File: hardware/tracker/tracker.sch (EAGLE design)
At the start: 2 parts, among them X1 MINI-USB-SHIELD-UX60-MB-5ST

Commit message: Parts libraries started
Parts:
- added U$2: BMP085, bmp085:BMP085
- added U$3: CC2540-MINI-BLE, cc2540:CC2540-MINI-BLE
- X1: value MINI-USB-SHIELD-UX60-MB-5ST -> MINI-USB-SCHIELD-32005-301; device con-hirose:MINI-USB-SHIELD-UX60-MB-5ST -> con-cypressindustries:MINI-USB-SCHIELD-32005-301
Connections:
- new net +5V: X1G$1.1
- new net GND: X1G$1.5, X1S.S1, X1S.S2, X1S.S3, X1S.S4
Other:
- moved on the sheet: U$1
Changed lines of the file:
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@@
 <grid distance="0.1" unitdist="inch" unit="inch" style="lines" multiple="1" display="no" altdistance="0.01" altunitdist="inch" altunit="inch"/>
 <layers>
-<layer number="1" name="Top" color="4" fill="1" visible="yes" active="no"/>
-<layer number="16" name="Bottom" color="1" fill="1" visible="yes" active="no"/>
-<layer number="17" name="Pads" color="2" fill="1" visible="yes" active="no"/>
-<layer number="18" name="Vias" color="2" fill="1" visible="yes" active="no"/>
-<layer number="19" name="Unrouted" color="6" fill="1" visible="yes" active="no"/>
-<layer number="20" name="Dimension" color="15" fill="1" visible="yes" active="no"/>
-<layer number="21" name="tPlace" color="7" fill="1" visible="yes" active="no"/>
-<layer number="22" name="bPlace" color="7" fill="1" visible="yes" active="no"/>
-<layer number="23" name="tOrigins" color="15" fill="1" visible="yes" active="no"/>
-<layer number="24" name="bOrigins" color="15" fill="1" visible="yes" active="no"/>
-<layer number="25" name="tNames" color="7" fill="1" visible="yes" active="no"/>
-<layer number="26" name="bNames" color="7" fill="1" visible="yes" active="no"/>
-<layer number="27" name="tValues" color="7" fill="1" visible="yes" active="no"/>
-<layer number="28" name="bValues" color="7" fill="1" visible="yes" active="no"/>
+<layer number="1" name="Top" color="4" fill="1" visible="no" active="no"/>
+<layer number="16" name="Bottom" color="1" fill="1" visible="no" active="no"/>
+<layer number="17" name="Pads" color="2" fill="1" visible="no" active="no"/>
+<layer number="18" name="Vias" color="2" fill="1" visible="no" active="no"/>
+<layer number="19" name="Unrouted" color="6" fill="1" visible="no" active="no"/>
+<layer number="20" name="Dimension" color="15" fill="1" visible="no" active="no"/>
+<layer number="21" name="tPlace" color="7" fill="1" visible="no" active="no"/>
+<layer number="22" name="bPlace" color="7" fill="1" visible="no" active="no"/>
+<layer number="23" name="tOrigins" color="15" fill="1" visible="no" active="no"/>
+<layer number="24" name="bOrigins" color="15" fill="1" visible="no" active="no"/>
+<layer number="25" name="tNames" color="7" fill="1" visible="no" active="no"/>
+<layer number="26" name="bNames" color="7" fill="1" visible="no" active="no"/>
+<layer number="27" name="tValues" color="7" fill="1" visible="no" active="no"/>
+<layer number="28" name="bValues" color="7" fill="1" visible="no" active="no"/>
 <layer number="29" name="tStop" color="7" fill="3" visible="no" active="no"/>
 <layer number="30" name="bStop" color="7" fill="6" visible="no" active="no"/>
@@
 <layer number="35" name="tGlue" color="7" fill="4" visible="no" active="no"/>
 <layer number="36" name="bGlue" color="7" fill="5" visible="no" active="no"/>
-<layer number="37" name="tTest" color="7" fill="1" visible="yes" active="no"/>
-<layer number="38" name="bTest" color="7" fill="1" visible="yes" active="no"/>
+<layer number="37" name="tTest" color="7" fill="1" visible="no" active="no"/>
+<layer number="38" name="bTest" color="7" fill="1" visible="no" active="no"/>
 <layer number="39" name="tKeepout" color="4" fill="11" visible="no" active="no"/>
 <layer number="40" name="bKeepout" color="1" fill="11" visible="no" active="no"/>
@@
 <layer number="44" name="Drills" color="7" fill="1" visible="no" active="no"/>
 <layer number="45" name="Holes" color="7" fill="1" visible="no" active="no"/>
-<layer number="46" name="Milling" color="3" fill="1" visible="yes" active="no"/>
-<layer number="47" name="Measures" color="7" fill="1" visible="yes" active="no"/>
-<layer number="48" name="Document" color="7" fill="1" visible="yes" active="no"/>
-<layer number="49" name="Reference" color="7" fill="1" visible="yes" active="no"/>
-<layer number="51" name="tDocu" color="7" fill="1" visible="yes" active="no"/>
-<layer number="52" name="bDocu" color="7" fill="1" visible="yes" active="no"/>
+<layer number="46" name="Milling" color="3" fill="1" visible="no" active="no"/>
+<layer number="47" name="Measures" color="7" fill="1" visible="no" active="no"/>
+<layer number="48" name="Document" color="7" fill="1" visible="no" active="no"/>
+<layer number="49" name="Reference" color="7" fill="1" visible="no" active="no"/>
+<layer number="51" name="tDocu" color="7" fill="1" visible="no" active="no"/>
+<layer number="52" name="bDocu" color="7" fill="1" visible="no" active="no"/>
 <layer number="91" name="Nets" color="2" fill="1" visible="yes" active="yes"/>
 <layer number="92" name="Busses" color="1" fill="1" visible="yes" active="yes"/>
@@
 <class number="0" name="default" width="0" drill="0">
 </class>
+<class number="1" name="VCC" width="0.3" drill="0">
+</class>
+<class number="2" name="GND" width="0.5" drill="0">
+</class>
+<class number="3" name="+5V" width="0.5" drill="0">
+</class>
 </classes>
 <parts>
-<part name="X1" library="con-hirose" deviceset="MINI-USB-SHIELD-" device="UX60-MB-5ST"/>
 <part name="U$1" library="adxl345" deviceset="ADXL345" device=""/>
+<part name="X1" library="con-cypressindustries" deviceset="MINI-USB-SCHIELD-" device="32005-301"/>
+<part name="GND1" library="supply1" deviceset="GND" device=""/>
+<part name="U$3" library="cc2540" deviceset="CC2540-MINI-BLE" device=""/>
+<part name="P+1" library="supply1" deviceset="VCC" device=""/>
+<part name="+3V1" library="supply1" deviceset="+3V3" device=""/>
+<part name="P+2" library="supply1" deviceset="+5V" device=""/>
+<part name="GND2" library="supply1" deviceset="GND" device=""/>
+<part name="U$2" library="bmp085" deviceset="BMP085" device=""/>
 </parts>
 <sheets>
@@
 </plain>
 <instances>
-<instance part="X1" gate="G$1" x="17.78" y="-15.24" rot="MR0"/>
-<instance part="U$1" gate="G$1" x="96.52" y="-7.62"/>
+<instance part="U$1" gate="G$1" x="160.02" y="71.12"/>
+<instance part="X1" gate="G$1" x="20.32" y="0" smashed="yes" rot="R180"/>
+<instance part="X1" gate="S" x="20.32" y="-10.16" rot="MR0"/>
+<instance part="GND1" gate="1" x="17.78" y="-17.78"/>
+<instance part="U$3" gate="G$1" x="91.44" y="71.12"/>
+<instance part="P+1" gate="VCC" x="50.8" y="17.78"/>
+<instance part="+3V1" gate="G$1" x="66.04" y="20.32"/>
+<instance part="P+2" gate="1" x="35.56" y="-5.08" rot="R270"/>
+<instance part="GND2" gate="1" x="35.56" y="5.08" rot="R90"/>
+<instance part="U$2" gate="G$1" x="111.76" y="2.54"/>
 </instances>
 <busses>
 </busses>
 <nets>
+<net name="GND" class="0">
+<segment>
+<pinref part="X1" gate="S" pin="S4"/>
+<wire x1="15.24" y1="-12.7" x2="15.24" y2="-15.24" width="0.1524" layer="91"/>
+<pinref part="X1" gate="S" pin="S1"/>
+<wire x1="15.24" y1="-15.24" x2="17.78" y2="-15.24" width="0.1524" layer="91"/>
+<wire x1="17.78" y1="-15.24" x2="20.32" y2="-15.24" width="0.1524" layer="91"/>
+<wire x1="20.32" y1="-15.24" x2="22.86" y2="-15.24" width="0.1524" layer="91"/>
+<wire x1="22.86" y1="-15.24" x2="22.86" y2="-12.7" width="0.1524" layer="91"/>
+<pinref part="X1" gate="S" pin="S3"/>
+<wire x1="17.78" y1="-12.7" x2="17.78" y2="-15.24" width="0.1524" layer="91"/>
+<pinref part="X1" gate="S" pin="S2"/>
+<wire x1="20.32" y1="-12.7" x2="20.32" y2="-15.24" width="0.1524" layer="91"/>
+<pinref part="GND1" gate="1" pin="GND"/>
+<junction x="17.78" y="-15.24"/>
+<junction x="20.32" y="-15.24"/>
+</segment>
+<segment>
+<pinref part="X1" gate="G$1" pin="5"/>
+<pinref part="GND2" gate="1" pin="GND"/>
+<wire x1="33.02" y1="5.08" x2="25.4" y2="5.08" width="0.1524" layer="91"/>
+</segment>
+</net>
+<net name="+5V" class="0">
+<segment>
+<pinref part="X1" gate="G$1" pin="1"/>
+<pinref part="P+2" gate="1" pin="+5V"/>
+<wire x1="33.02" y1="-5.08" x2="25.4" y2="-5.08" width="0.1524" layer="91"/>
+</segment>
+</net>
 </nets>
 </sheet>

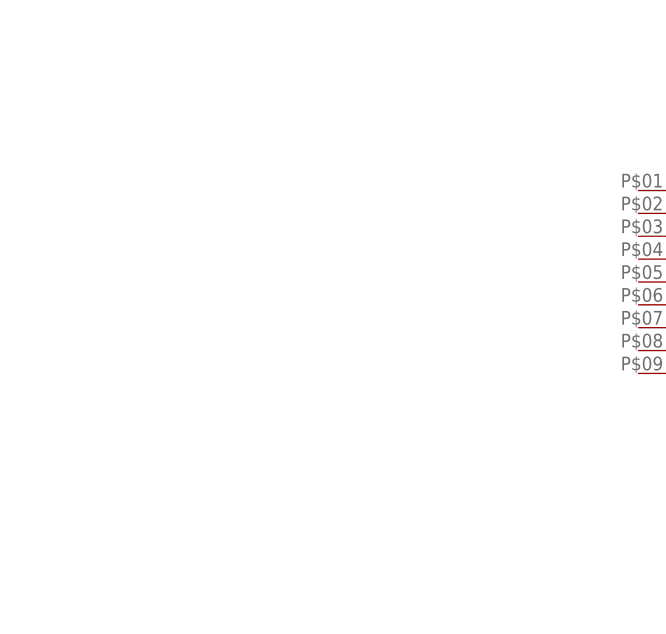
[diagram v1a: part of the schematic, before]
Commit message: FGPMMOPA6C GPS Standalone Module added
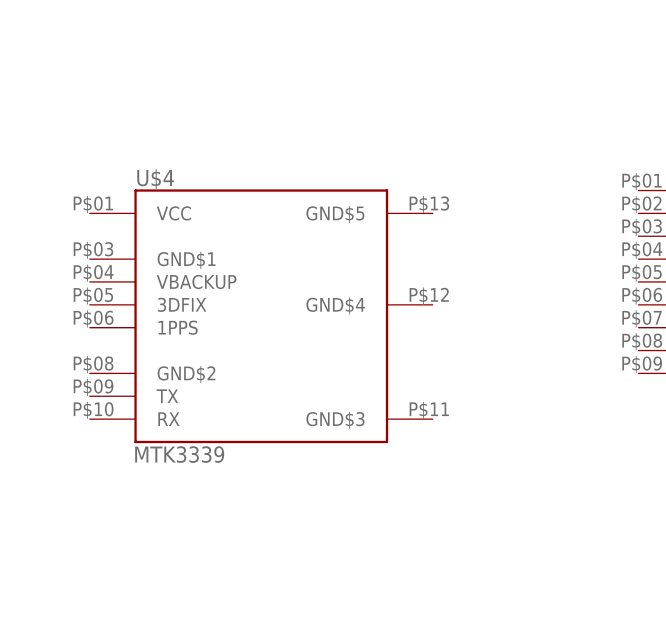
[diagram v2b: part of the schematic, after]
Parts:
- added U$4: MTK3339, mtk3339:MTK3339
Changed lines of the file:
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@@
 <part name="GND2" library="supply1" deviceset="GND" device=""/>
 <part name="U$2" library="bmp085" deviceset="BMP085" device=""/>
+<part name="U$4" library="mtk3339" deviceset="MTK3339" device=""/>
 </parts>
 <sheets>
@@
 <instance part="GND2" gate="1" x="35.56" y="5.08" rot="R90"/>
 <instance part="U$2" gate="G$1" x="111.76" y="2.54"/>
+<instance part="U$4" gate="G$1" x="20.32" y="76.2"/>
 </instances>
 <busses>

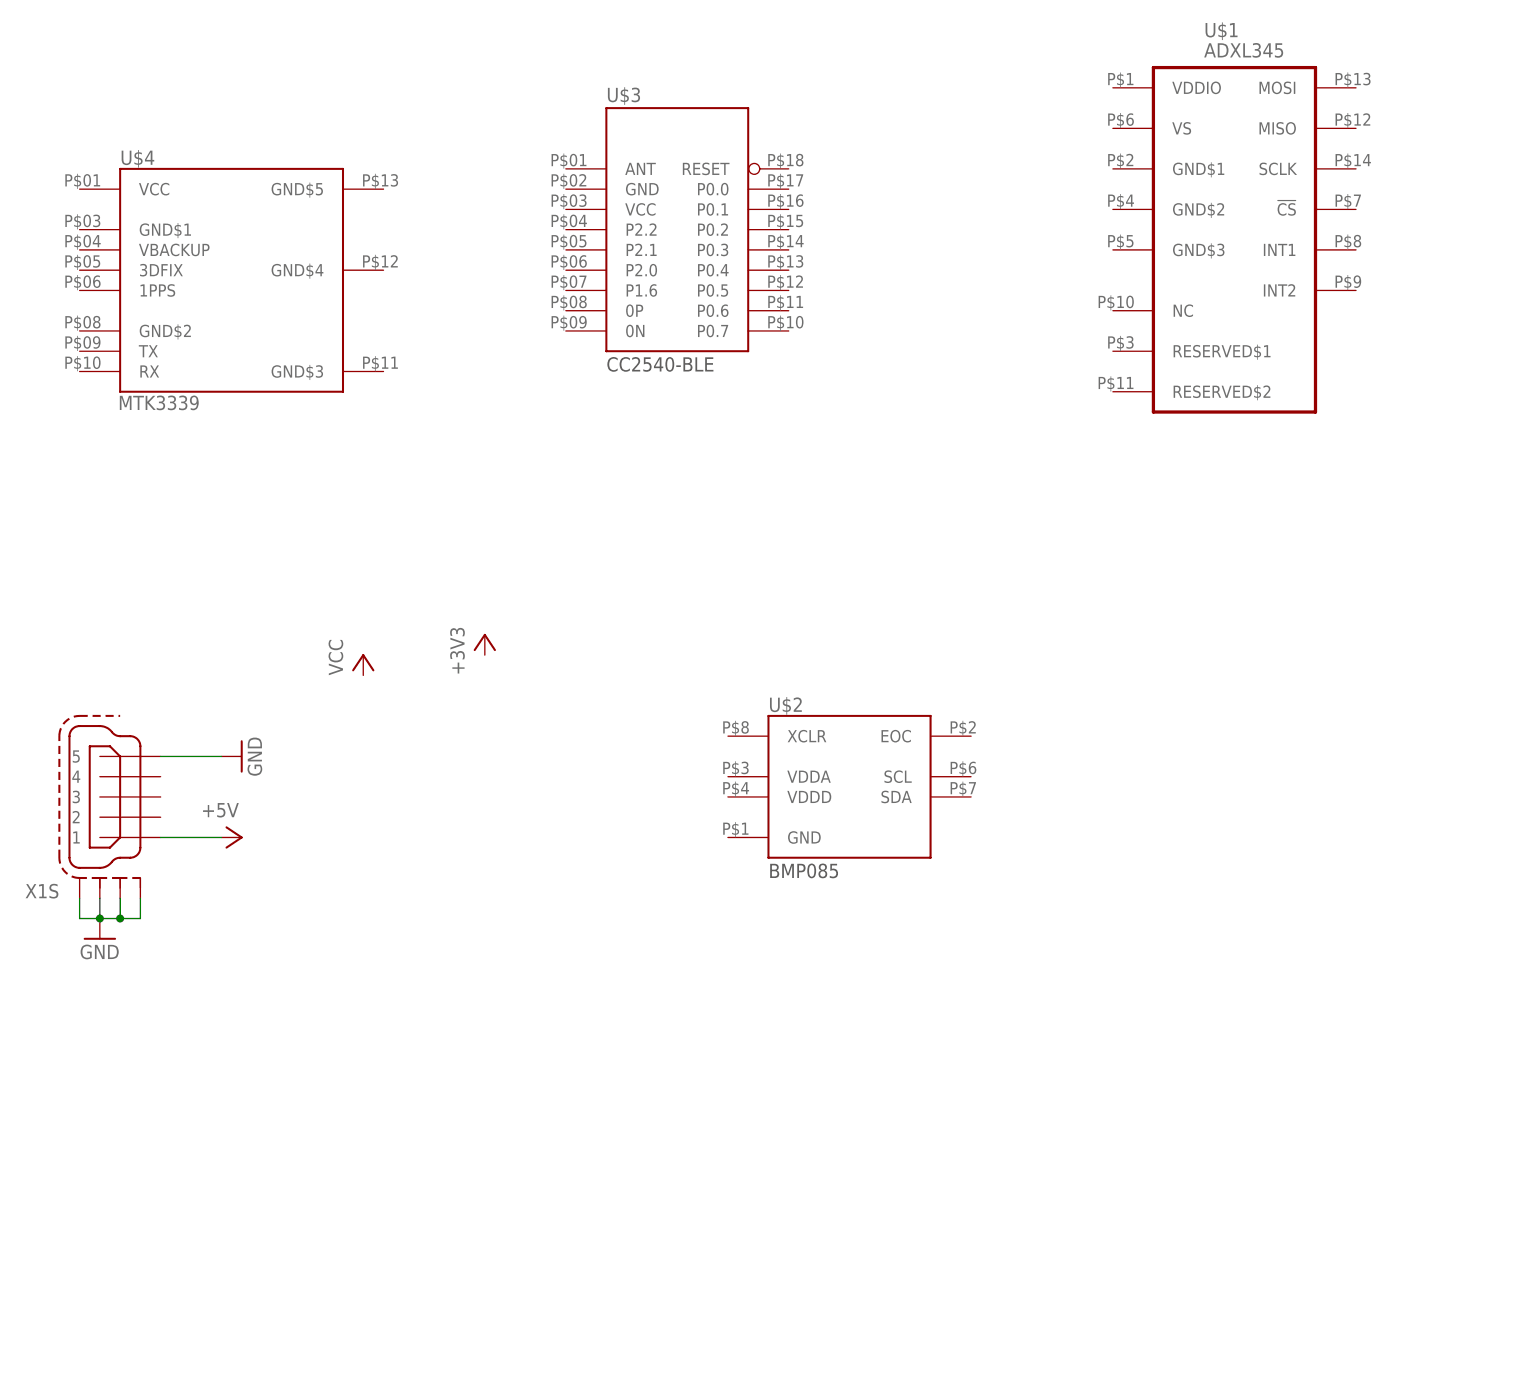
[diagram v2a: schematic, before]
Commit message: Added KCSA02 and KCSC02 LED modules
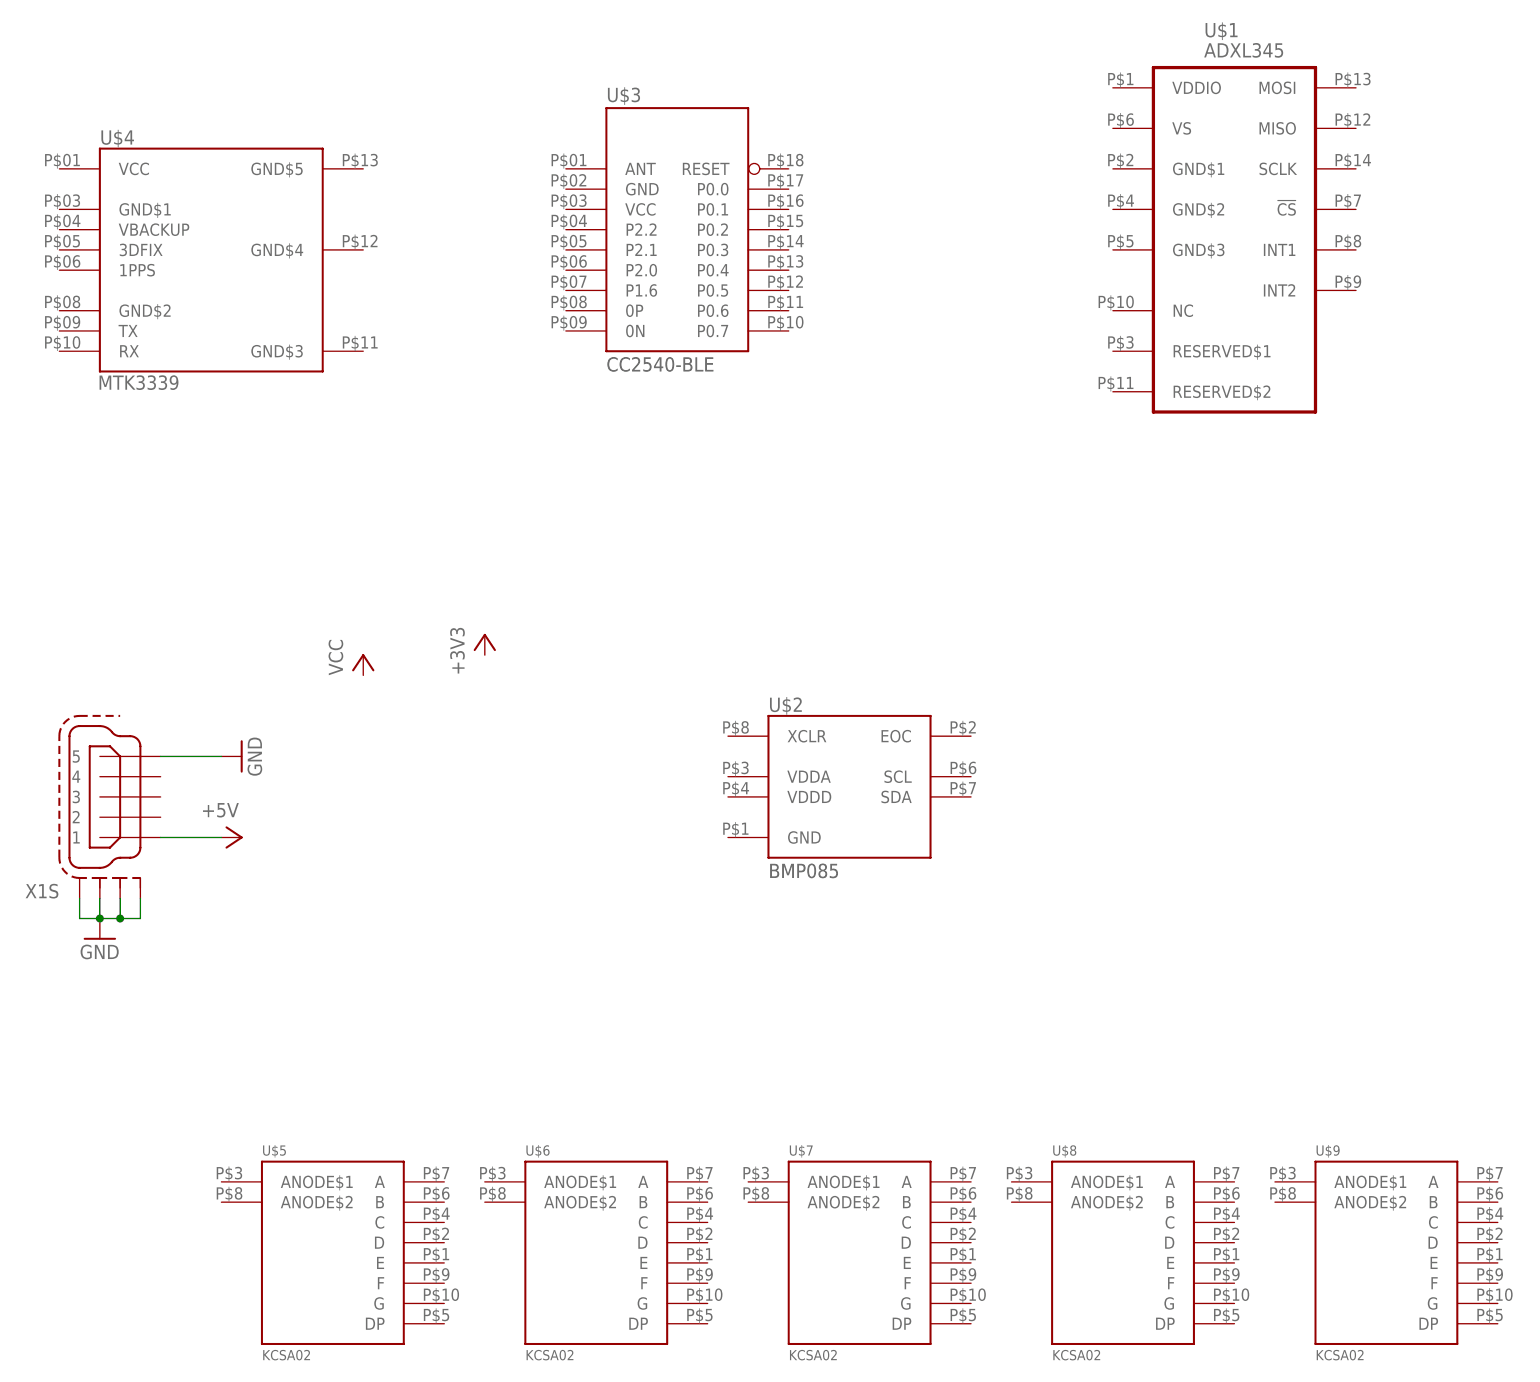
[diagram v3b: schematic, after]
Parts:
- added U$5, U$6, U$7, U$8, U$9: KCSA02-109-SMALL, kcsx02:KCSA02-109-SMALL
- U$4: device mtk3339:MTK3339 -> FGPMMOPA6C:MTK3339
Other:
- moved on the sheet: U$4
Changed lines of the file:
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@@
 <part name="GND2" library="supply1" deviceset="GND" device=""/>
 <part name="U$2" library="bmp085" deviceset="BMP085" device=""/>
-<part name="U$4" library="mtk3339" deviceset="MTK3339" device=""/>
+<part name="U$4" library="FGPMMOPA6C" deviceset="MTK3339" device=""/>
+<part name="U$5" library="kcsx02" deviceset="KCSA02-109" device="-SMALL"/>
+<part name="U$6" library="kcsx02" deviceset="KCSA02-109" device="-SMALL"/>
+<part name="U$7" library="kcsx02" deviceset="KCSA02-109" device="-SMALL"/>
+<part name="U$8" library="kcsx02" deviceset="KCSA02-109" device="-SMALL"/>
+<part name="U$9" library="kcsx02" deviceset="KCSA02-109" device="-SMALL"/>
 </parts>
 <sheets>
@@
 <instance part="GND2" gate="1" x="35.56" y="5.08" rot="R90"/>
 <instance part="U$2" gate="G$1" x="111.76" y="2.54"/>
-<instance part="U$4" gate="G$1" x="20.32" y="76.2"/>
+<instance part="U$4" gate="G$1" x="33.02" y="68.58"/>
+<instance part="U$5" gate="G$1" x="45.72" y="-55.88"/>
+<instance part="U$6" gate="G$1" x="78.74" y="-55.88"/>
+<instance part="U$7" gate="G$1" x="111.76" y="-55.88"/>
+<instance part="U$8" gate="G$1" x="144.78" y="-55.88"/>
+<instance part="U$9" gate="G$1" x="177.8" y="-55.88"/>
 </instances>
 <busses>

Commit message: no message
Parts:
- added BTN1, BTN2: FLAT-BUTTON, ml:FLAT-BUTTON
- added C2, C3, C4: 10uF, resistor:CPOL-EUB
- added D1, D2: (no value), diode:DIODE-SOD106-R
- added IC1: TP4056, TP4056:TP4056
- added IC2: LM1117MPX-3.3, lm1117:LM1117MPX-3.3
- added R1: PROG, resistor:R-EU_M0805
- added SW1: PWR-SWITCH, ml:PWR-SWITCH
- added U$10: ADXL345, adxl345:ADXL345
- added U$11: CC2540-MINI-BLE, cc2540:CC2540-MINI-BLE
- added U$12: MICROSD, micro-sd:MICROSD
- U$1: value ADXL345 -> KCSA02-109-SMALL; device adxl345:ADXL345 -> kcsx02:KCSA02-109-SMALL
- U$2: value BMP085 -> KCSA02-109-SMALL; device bmp085:BMP085 -> kcsx02:KCSA02-109-SMALL
- U$3: value CC2540-MINI-BLE -> KCSA02-109-SMALL; device cc2540:CC2540-MINI-BLE -> kcsx02:KCSA02-109-SMALL
- U$4: value MTK3339 -> KCSA02-109-SMALL; device FGPMMOPA6C:MTK3339 -> kcsx02:KCSA02-109-SMALL
- U$6: value KCSA02-109-SMALL -> BATTERY+; device kcsx02:KCSA02-109-SMALL -> ml:BATTERY+
- U$7: value KCSA02-109-SMALL -> BATTERY-; device kcsx02:KCSA02-109-SMALL -> ml:BATTERY-
- U$8: value KCSA02-109-SMALL -> FGPMMOPA6C; device kcsx02:KCSA02-109-SMALL -> FGPMMOPA6C:FGPMMOPA6C
- U$9: value KCSA02-109-SMALL -> BMP085; device kcsx02:KCSA02-109-SMALL -> bmp085:BMP085
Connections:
- new net +3V3: C3.+, IC2.OUT, IC2.OUT1
- new net A: U$1.A, U$2.A, U$3.A, U$4.A, U$5.A
- new net B: U$1.B, U$2.B, U$3.B, U$4.B, U$5.B
- new net BAT+: C2.+, D2.A, IC1.BAT, U$6.BATTERY+#1, U$6.BATTERY+#2
- new net BAT-PROG: IC1.PROG, R1.2
- new net C: U$1.C, U$2.C, U$3.C, U$4.C, U$5.C
- new net CHARGER_CHARGING: IC1.CHRG
- new net CHARGER_ENABLE: IC1.CE
- new net CHARGER_STANDBY: IC1.STDBY
- new net D: U$1.D, U$2.D, U$3.D, U$4.D, U$5.D
- new net E: U$1.E, U$2.E, U$3.E, U$4.E, U$5.E
- new net F: U$1.F, U$2.F, U$3.F, U$4.F, U$5.F
- new net G: U$1.G, U$2.G, U$3.G, U$4.G, U$5.G
- new net H: U$1.DP, U$2.DP, U$3.DP, U$4.DP, U$5.DP
- new net N$2: U$1.ANODE$1, U$1.ANODE$2
- new net N$3: U$2.ANODE$1, U$2.ANODE$2
- new net N$4: U$3.ANODE$1, U$3.ANODE$2
- new net N$5: U$4.ANODE$1, U$4.ANODE$2
- new net N$6: U$5.ANODE$1, U$5.ANODE$2
- new net N$7: D1.C, D2.C, SW1.PWR-IN
- new net N$8: IC2.IN, SW1.PWR-OUT1
- new net USB+D: X1G$1.3
- new net USB-D: X1G$1.2
- net +5V: now also C4.+, D1.A, IC1.VCC
- net GND: now also C2.-, C3.-, C4.-, IC1.GND, IC1.TEMP, IC2.GND, R1.1, SW1.SHIELD@1, SW1.SHIELD@2, SW1.SHIELD@3, U$10.GND@1, U$10.GND@2, U$10.GND@3, U$11.GND, U$7.BATTERY-@1, U$7.BATTERY-@2, U$7.BATTERY-@3, U$8.GND@1, U$8.GND@2, U$8.GND@3, U$8.GND@4, U$8.GND@5, U$9.GND
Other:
- moved on the sheet: U$5, X1S
